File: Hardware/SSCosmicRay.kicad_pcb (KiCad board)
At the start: 2 copper layers, 60 x 39 mm, 111 parts, among them J1 ICSP-PIC, J2 USB_MINI, SW1 PGM, SW2 RST, U1 MAX4477, U2 MAX4477, U3 MAX991, U4 741G08, U5 PIC32MX250F128B, U6 MAX4477, U7 MAX4477, U8 LTC3129-SOP, U9 AOZ1280, X1 8MHz

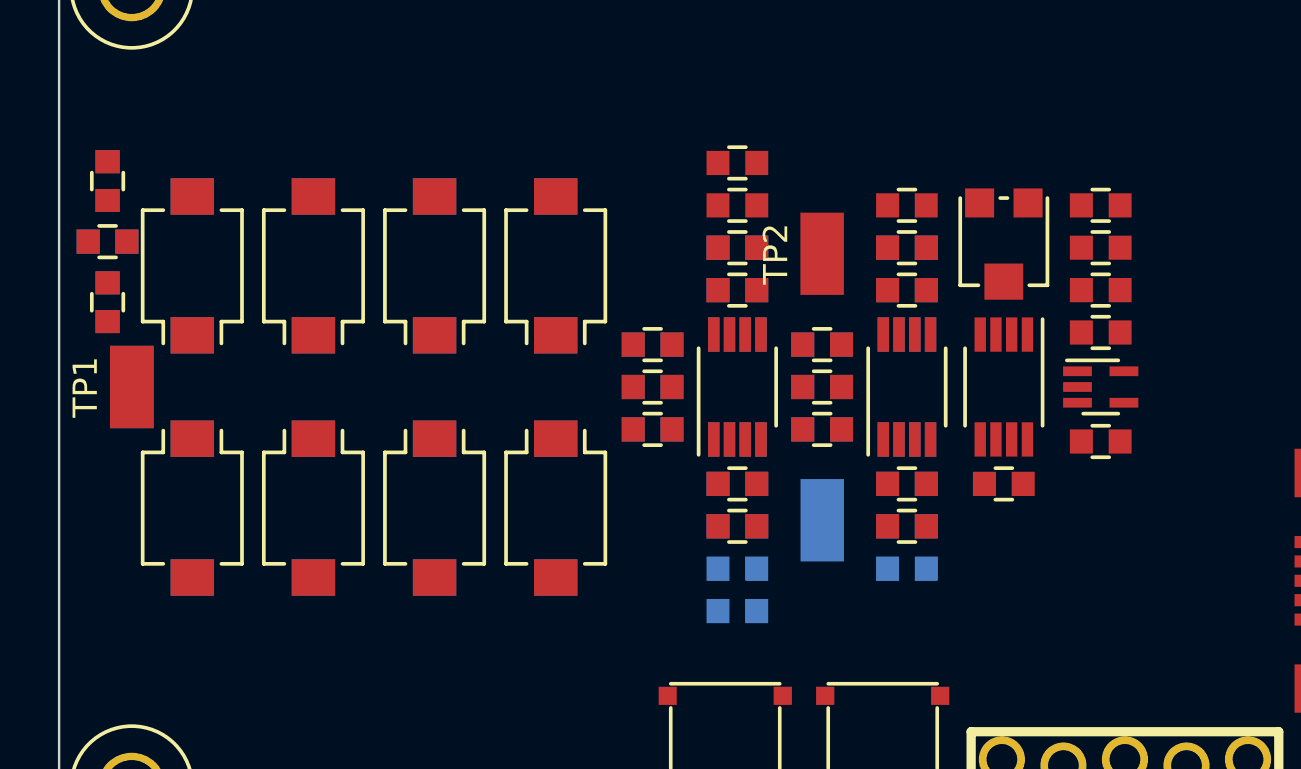
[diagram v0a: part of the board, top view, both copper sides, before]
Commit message: Reroute signal chain with IPC spacing
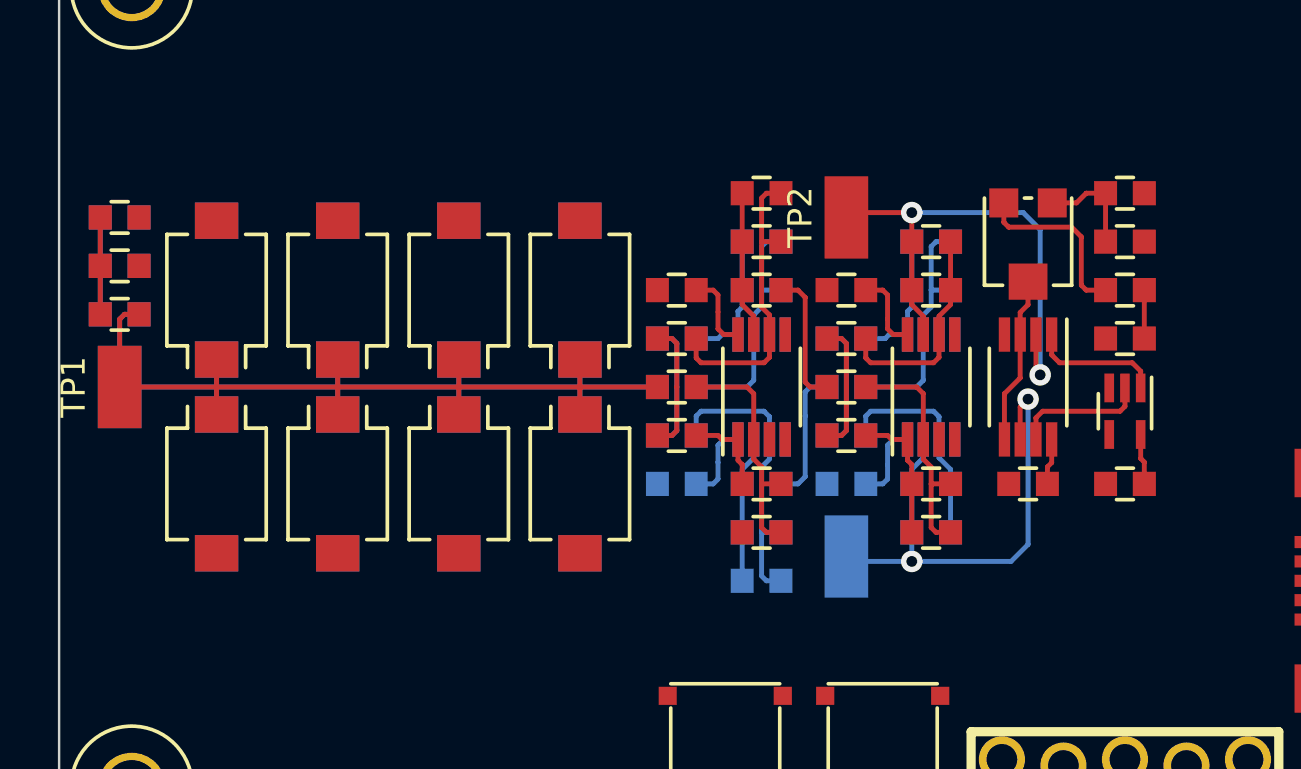
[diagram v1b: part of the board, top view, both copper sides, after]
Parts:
- moved C15 5.84 mm to (167.5, 70.0)
- moved C22 5.81 mm to (149.0, 82.0), turned to 180 degrees
- moved C3 5.81 mm to (149.0, 74.0), turned to 180 degrees
- moved C25 4.30 mm to (156.0, 82.0), turned to 180 degrees
- moved C6 4.30 mm to (156.0, 74.0), turned to 180 degrees
- moved C13 3.88 mm to (167.5, 76.0)
- moved R10 3.64 mm to (167.5, 74.0)
- moved R11 2.24 mm to (167.5, 72.0)
- moved C14 2.02 mm to (167.5, 82.0)
- moved TP2 1.80 mm to (156.0, 71.0)
- moved TP4 1.80 mm to (156.0, 85.0)
- moved R1 1.58 mm to (126.0, 71.0), turned to 0 degrees
- moved R23 1.58 mm to (126.0, 71.0), turned to 0 degrees
- moved D1 1.41 mm to (130.0, 74.0)
- moved D10 1.41 mm to (130.0, 82.0)
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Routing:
- net /Amplifier 2/In: track 0.00 -> 35.0 mm
- net /Amplifier 1/In: track 0.00 -> 35.0 mm
- net /Processor/A1: track 0.00 -> 21.3 mm, vias 0 -> 2
- net /Processor/A2: track 0.00 -> 20.9 mm, vias 0 -> 2
- net +3.3V: track 0.00 -> 19.2 mm
- net N-0000057: track 0.00 -> 12.4 mm
- net N-0000017: track 0.00 -> 12.4 mm
- net N-0000059: track 0.00 -> 9.83 mm
- net N-0000053: track 0.00 -> 9.83 mm
- net N-0000019: track 0.00 -> 9.83 mm
- net N-0000014: track 0.00 -> 9.83 mm
- net N-0000052: track 0.00 -> 8.97 mm
- net N-0000012: track 0.00 -> 8.97 mm
- net N-0000024: track 0.00 -> 7.33 mm
- net N-0000022: track 0.00 -> 6.92 mm
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
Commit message: Power sections
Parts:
- added R30: 10k, RESC1608-N, B.Cu at (205.0, 65.5)
- C18, C32, C33, C34, C36: footprint CAPC2012-N -> CAPC1608-N
- C38, D17, L2, R27, R28, R29, U9: moved to B.Cu
- C39: value C -> 10uF; footprint CAPC2012-N -> CAPC1608-N; moved to B.Cu
- C40: footprint CAPC2012-N -> CAPC1608-N; moved to B.Cu
- moved C32 54.4 mm to (216.5, 67.5), turned to 180 degrees
- moved C33 53.4 mm to (216.5, 59.5), turned to 180 degrees
- moved R25 52.9 mm to (205.0, 61.5), turned to 0 degrees
- moved C34 52.6 mm to (210.5, 67.5)
- moved R26 52.5 mm to (205.0, 63.5), turned to 180 degrees
- moved U8 52.5 mm to (210.5, 63.5)
- moved C36 52.3 mm to (210.5, 59.5)
- moved C37 51.9 mm to (205.0, 67.5), turned to 180 degrees
- moved L1 51.0 mm to (216.5, 63.5)
- moved C35 50.7 mm to (205.0, 59.5), turned to 180 degrees
- moved L2 11.8 mm to (194.0, 65.5)
- moved D17 9.75 mm to (198.5, 65.0)
- moved C39 8.81 mm to (189.5, 62.5), turned to 0 degrees
- moved C38 6.25 mm to (194.0, 62.5)
- moved C40 5.03 mm to (198.5, 60.5), turned to 0 degrees
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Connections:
- U8 pad 2: VCOM -> N-0000064
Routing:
- net +12V: track 0.00 -> 15.0 mm
- net GND: track 0.00 -> 13.5 mm, vias 0 -> 6
- net N-0000072: track 0.00 -> 11.3 mm
- net N-0000071: track 0.00 -> 8.45 mm
- net /Power/BS2: track 0.00 -> 5.62 mm
- net VCOM: track 0.00 -> 5.57 mm
- net /Power/BS1: track 0.00 -> 5.17 mm
- net /Power/SW2: track 0.00 -> 4.65 mm
- net N-0000065: track 0.00 -> 4.47 mm
- net /Power/SW1: track 0.00 -> 4.15 mm
- net N-0000064: track 0.00 -> 2.85 mm
- net N-0000069: track 0.00 -> 2.47 mm
- net N-0000062: track 0.00 -> 2.24 mm
- net /Power/Lx: track 0.00 -> 2.24 mm
- added copper zone on B.Cu, net +12V
- added copper zone on B.Cu, net +3.3V
- added copper zone on B.Cu, net /Power/Lx
- added copper zone on B.Cu, net /Power/SW1
- added copper zone on B.Cu, net /Power/SW2
- added copper zone on B.Cu, net GND
- added copper zone on B.Cu, net VCOM

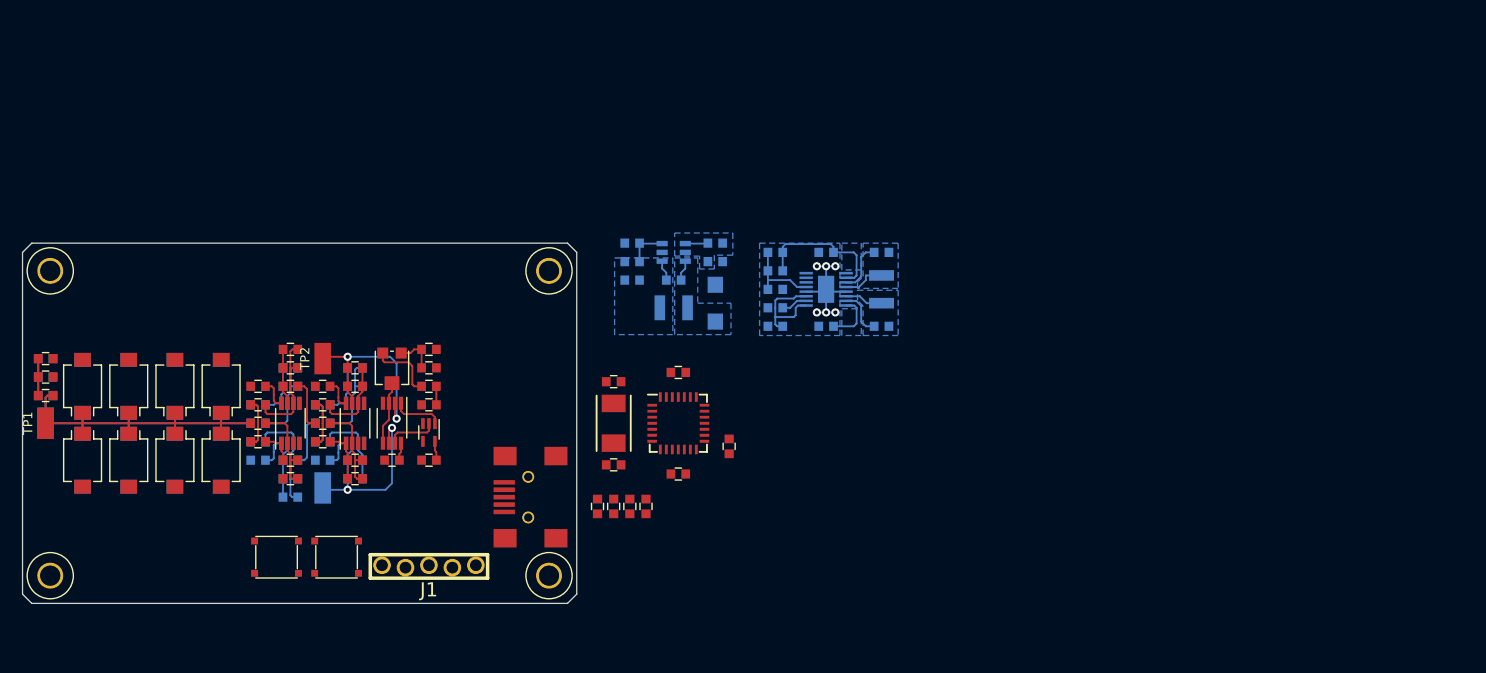
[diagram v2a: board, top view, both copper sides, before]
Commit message: Switch to larger enclosure
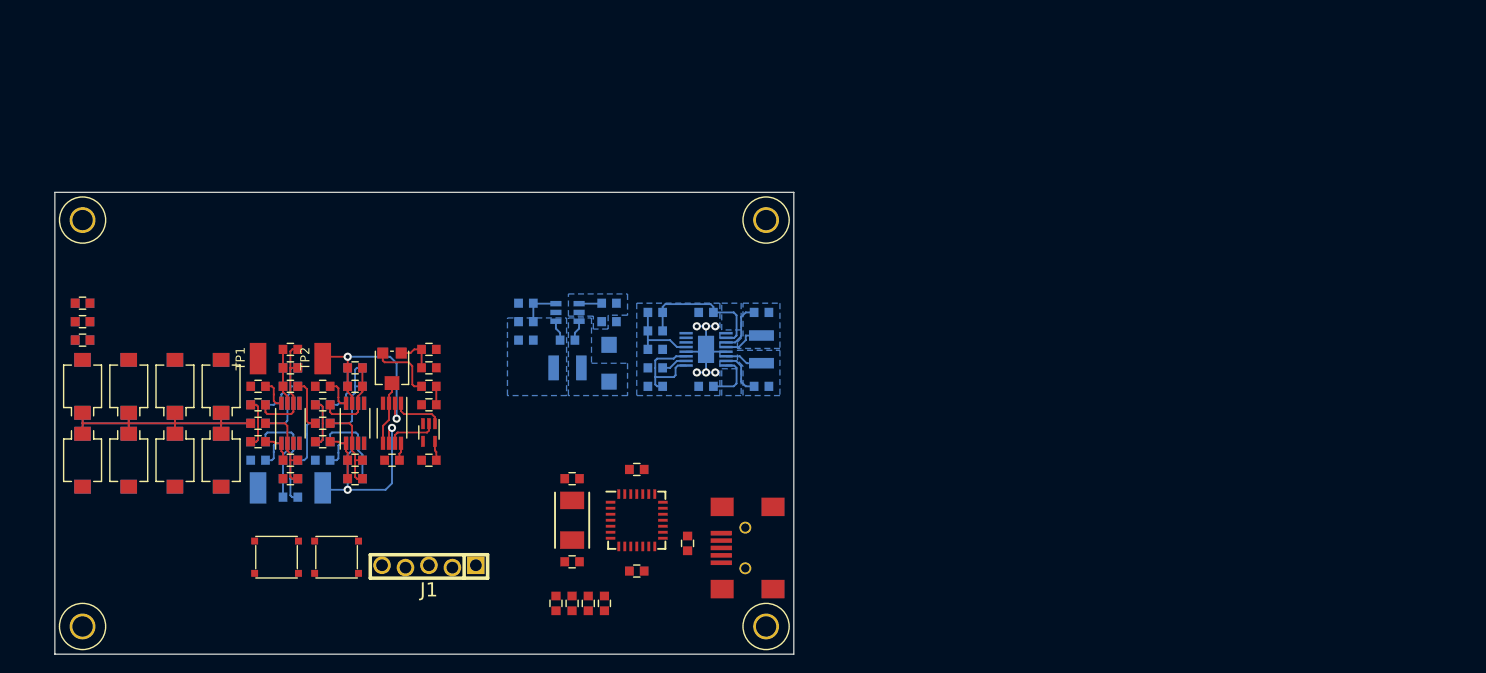
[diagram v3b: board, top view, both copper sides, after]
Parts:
- moved J2 24.1 mm to (207.0, 91.5)
- moved MECH-HOLE220 24.1 mm to (204.0, 56.0)
- moved MECH-HOLE220 24.1 mm to (204.0, 100.0)
- moved TP1 24.0 mm to (149.0, 71.0)
- moved TP3 24.0 mm to (149.0, 85.0)
- moved C32 14.5 mm to (203.5, 74.0)
- moved C33 14.5 mm to (203.5, 66.0)
- moved C34 14.5 mm to (197.5, 74.0)
- moved C35 14.5 mm to (192.0, 66.0)
- moved C36 14.5 mm to (197.5, 66.0)
- moved C37 14.5 mm to (192.0, 74.0)
- moved L1 14.5 mm to (203.5, 70.0)
- moved R25 14.5 mm to (192.0, 68.0)
- moved R26 14.5 mm to (192.0, 70.0)
- moved R30 14.5 mm to (192.0, 72.0)
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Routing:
- net /Amplifier 2/In: track 35.0 -> 27.3 mm
- net /Amplifier 1/In: track 35.0 -> 27.3 mm
- net N-0000061: track 4.00 -> 0.00 mm
- net N-0000010: track 4.00 -> 0.00 mm
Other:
- board size 60 x 39 mm -> 80 x 50 mm
- board text added: "To Fit Hammond 1455C802"
- board text removed: "To Fit Hammond 1455D602"

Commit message: Fully route signal chain
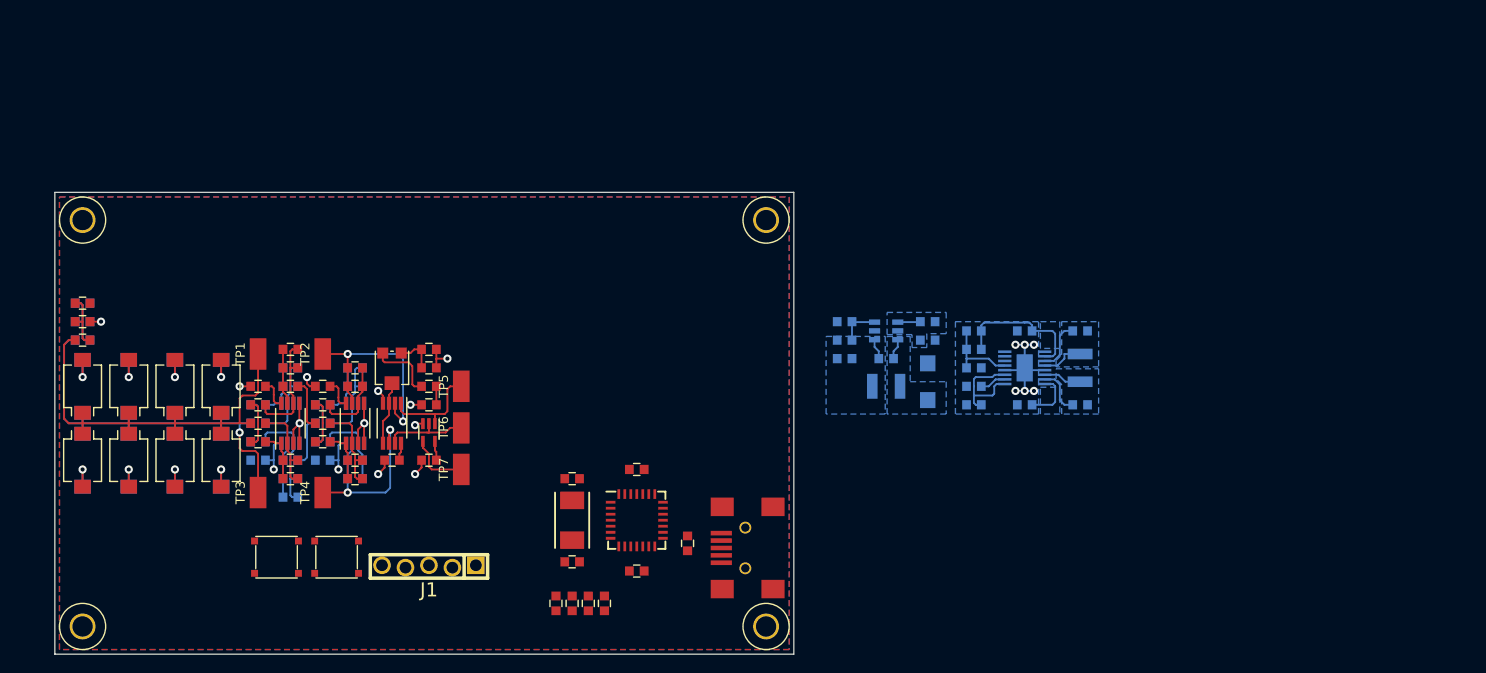
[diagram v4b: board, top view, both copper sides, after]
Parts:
- added TP5: TP, TP-5015, F.Cu at (171.0, 74.0)
- added TP6: TP, TP-5015, F.Cu at (171.0, 78.5)
- added TP7: TP, TP-5015, F.Cu at (171.0, 83.0)
- TP3, TP4: moved to F.Cu
- moved C32 34.6 mm to (238.0, 76.0)
- moved C33 34.6 mm to (238.0, 68.0)
- moved C34 34.6 mm to (232.0, 76.0)
- moved C35 34.6 mm to (226.5, 68.0)
- moved C36 34.6 mm to (232.0, 68.0)
- moved C37 34.6 mm to (226.5, 76.0)
- moved C38 34.6 mm to (217.0, 71.0)
- moved C39 34.6 mm to (212.5, 71.0)
- moved C40 34.6 mm to (221.5, 69.0)
- moved D17 34.6 mm to (221.5, 73.5)
- moved L1 34.6 mm to (238.0, 72.0)
- moved L2 34.6 mm to (217.0, 74.0)
- moved R25 34.6 mm to (226.5, 70.0)
- moved R26 34.6 mm to (226.5, 72.0)
- moved R27 34.6 mm to (221.5, 67.0)
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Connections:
- U4 pad 4: (no net) -> /Processor/C
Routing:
- net GND: track 13.5 -> 71.5 mm, vias 6 -> 25
- net /Amplifier 2/In: track 27.3 -> 48.0 mm, vias 0 -> 1
- net /Amplifier 1/In: track 27.3 -> 48.0 mm
- net /Processor/C: track 0.00 -> 6.63 mm
- net N-0000061: track 0.00 -> 6.17 mm
- net N-0000010: track 0.00 -> 6.17 mm
- net /Processor/C1: track 5.48 -> 11.2 mm
- net /Processor/C2: track 5.52 -> 9.35 mm
- net +3.3V: track 19.2 -> 21.5 mm, vias 0 -> 2
- net /Processor/A1: track 21.3 -> 23.6 mm
- net N-0000021: track 3.70 -> 5.70 mm
- added copper zone on F.Cu, net +3.3V
